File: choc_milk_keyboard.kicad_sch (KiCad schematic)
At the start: 6 parts, among them J1 Conn_01x02_Female, SW1 SW_PUSH, SW2 SW_PUSH, U1 ProMicro

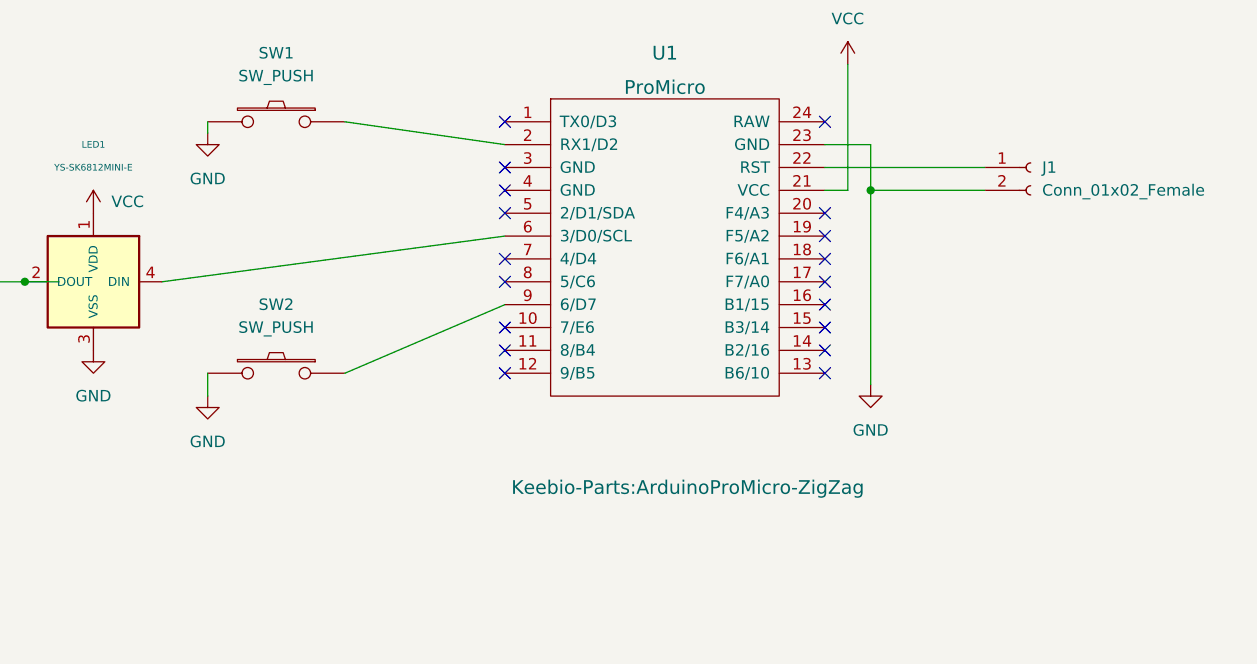
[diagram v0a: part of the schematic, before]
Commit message: Refactored for USB-C ProMicro USB-C is 3mm longer than micro usb Created a new footprint variant
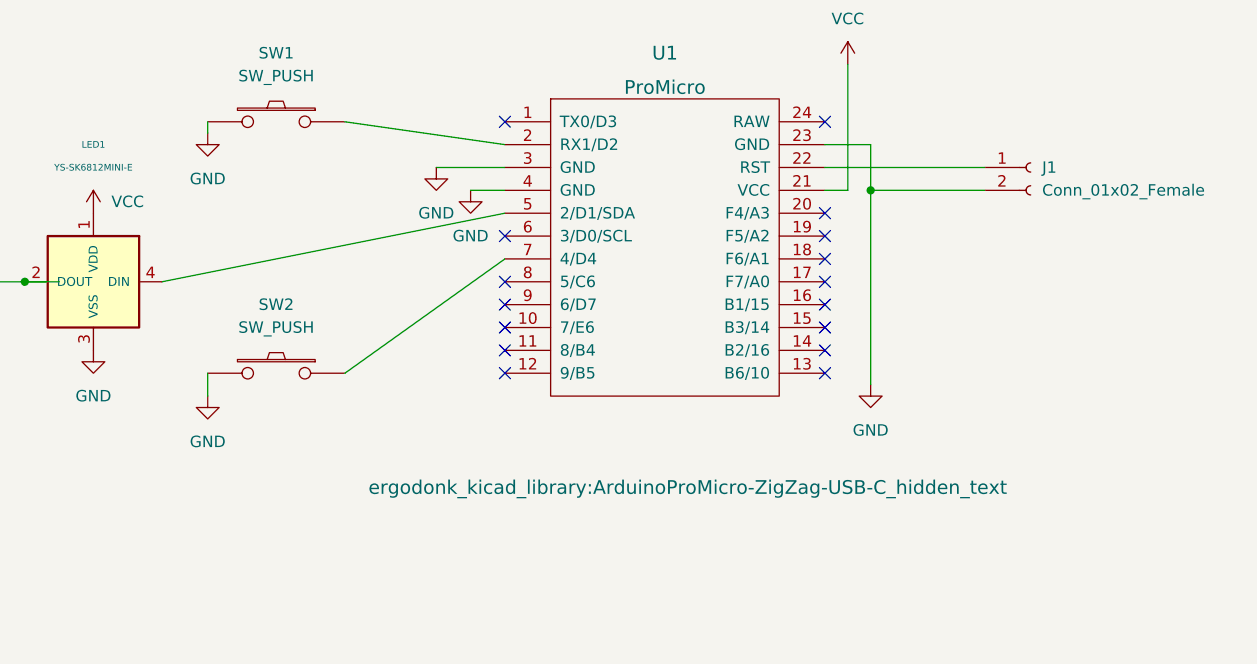
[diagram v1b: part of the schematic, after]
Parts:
- U1: footprint Keebio-Parts:ArduinoProMicro-ZigZag -> ergodonk_kicad_library:ArduinoProMicro-ZigZag-USB-C_hidden_text
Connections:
- net GND: now also U1.3 (GND), U1.4 (GND)
- net at U1.5 (2/D1/SDA): now also LED1.4 (DIN)
- net at U1.6 (3/D0/SCL): no longer LED1.4 (DIN)
- net at U1.7 (4/D4): now also SW2.1
- net at U1.9 (6/D7): no longer SW2.1
- no-connect marks 18 -> 16
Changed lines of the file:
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@@
   (no_connect (at 179.07 99.06))
   (no_connect (at 179.07 101.6))
-  (no_connect (at 143.51 78.74))
-  (no_connect (at 143.51 81.28))
-  (no_connect (at 143.51 83.82))
   (no_connect (at 143.51 96.52))
   (no_connect (at 143.51 99.06))
   (no_connect (at 143.51 101.6))
-  (no_connect (at 143.51 88.9))
   (no_connect (at 143.51 91.44))
-  (wire (pts (xy 125.73 101.6) (xy 143.51 93.98))
-    (stroke (width 0) (type default) (color 0 0 0 0))
-  )
+  (no_connect (at 143.51 93.98))
+  (no_connect (at 143.51 86.36))
   (wire (pts (xy 93.98 91.44) (xy 90.17 91.44))
     (stroke (width 0) (type default) (color 0 0 0 0))
@@
     (stroke (width 0) (type default) (color 0 0 0 0))
   )
+  (wire (pts (xy 135.89 78.74) (xy 143.51 78.74))
+    (stroke (width 0) (type default) (color 0 0 0 0))
+  )
   (wire (pts (xy 184.15 76.2) (xy 184.15 81.28))
     (stroke (width 0) (type default) (color 0 0 0 0))
@@
     (stroke (width 0) (type default) (color 0 0 0 0))
   )
+  (wire (pts (xy 125.73 101.6) (xy 143.51 88.9))
+    (stroke (width 0) (type default) (color 0 0 0 0))
+  )
   (wire (pts (xy 110.49 104.14) (xy 110.49 101.6))
     (stroke (width 0) (type default) (color 0 0 0 0))
@@
     (stroke (width 0) (type default) (color 0 0 0 0))
   )
-  (wire (pts (xy 143.51 86.36) (xy 105.41 91.44))
-    (stroke (width 0) (type default) (color 0 0 0 0))
-  )
   (wire (pts (xy 196.85 81.28) (xy 184.15 81.28))
     (stroke (width 0) (type default) (color 0 0 0 0))
@@
   )
   (wire (pts (xy 179.07 76.2) (xy 184.15 76.2))
+    (stroke (width 0) (type default) (color 0 0 0 0))
+  )
+  (wire (pts (xy 139.7 81.28) (xy 143.51 81.28))
+    (stroke (width 0) (type default) (color 0 0 0 0))
+  )
+  (wire (pts (xy 143.51 83.82) (xy 105.41 91.44))
     (stroke (width 0) (type default) (color 0 0 0 0))
   )
@@
     (pin "1")
   )
+  (symbol (lib_id "power:GND") (at 139.7 81.28 0) (unit 1)
+    (in_bom yes) (on_board yes) (fields_autoplaced)
+    (property "Reference" "#PWR0112" (id 0) (at 139.7 87.63 0)
+      (effects (font (size 1.27 1.27)) hide)
+    )
+    (property "Value" "GND" (id 1) (at 139.7 86.36 0))
+    (property "Footprint" "" (id 2) (at 139.7 81.28 0)
+      (effects (font (size 1.27 1.27)) hide)
+    )
+    (property "Datasheet" "" (id 3) (at 139.7 81.28 0)
+      (effects (font (size 1.27 1.27)) hide)
+    )
+    (pin "1")
+  )
   (symbol (lib_id "kbd:ProMicro") (at 161.29 87.63 0) (unit 1)
     (in_bom yes) (on_board yes) (fields_autoplaced)
@@
       (effects (font (size 1.524 1.524)))
     )
-    (property "Footprint" "Keebio-Parts:ArduinoProMicro-ZigZag" (id 2) (at 163.83 114.3 0)
+    (property "Footprint" "ergodonk_kicad_library:ArduinoProMicro-ZigZag-USB-C_hidden_text" (id 2) (at 163.83 114.3 0)
       (effects (font (size 1.524 1.524)))
     )
@@
     (pin "1")
   )
+  (symbol (lib_id "power:GND") (at 135.89 78.74 0) (unit 1)
+    (in_bom yes) (on_board yes) (fields_autoplaced)
+    (property "Reference" "#PWR0111" (id 0) (at 135.89 85.09 0)
+      (effects (font (size 1.27 1.27)) hide)
+    )
+    (property "Value" "GND" (id 1) (at 135.89 83.82 0))
+    (property "Footprint" "" (id 2) (at 135.89 78.74 0)
+      (effects (font (size 1.27 1.27)) hide)
+    )
+    (property "Datasheet" "" (id 3) (at 135.89 78.74 0)
+      (effects (font (size 1.27 1.27)) hide)
+    )
+    (pin "1")
+  )
   (symbol (lib_id "kbd:YS-SK6812MINI-E") (at 78.74 91.44 0) (mirror y) (unit 1)
     (in_bom yes) (on_board yes)
@@
       (reference "#PWR0110") (unit 1) (value "GND") (footprint "")
     )
+    (path "/5dadfc8f-3ee6-40da-896a-c632534f4a0e"
+      (reference "#PWR0111") (unit 1) (value "GND") (footprint "")
+    )
+    (path "/2e2b6378-1b23-4035-8bf1-41dbdbe8a392"
+      (reference "#PWR0112") (unit 1) (value "GND") (footprint "")
+    )
     (path "/08b252a0-3925-44b6-a676-7cbcf9d3501f"
       (reference "J1") (unit 1) (value "Conn_01x02_Female") (footprint "Connector_PinHeader_2.54mm:PinHeader_1x02_P2.54mm_Vertical")
@@
     )
     (path "/363f4179-68ab-4aea-9f89-f83afdbdb4b7"
-      (reference "U1") (unit 1) (value "ProMicro") (footprint "Keebio-Parts:ArduinoProMicro-ZigZag")
-    )
-  )
+      (reference "U1") (unit 1) (value "ProMicro") (footprint "ergodonk_kicad_library:ArduinoProMicro-ZigZag-USB-C_hidden_text")
+    )
+  )

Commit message: Added 3d models, flipped pro micro
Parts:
- SW1, SW2: footprint ergodonk_kicad_library:Low-Profile-Choc-MX -> ergodonk_kicad_library:Low-Profile-Choc-MX_no_text
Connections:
- net at U1.20 (F4/A3): now also LED1.4 (DIN)
- net at U1.5 (2/D1/SDA): no longer LED1.4 (DIN)
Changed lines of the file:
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@@
+    (stroke (width 0) (type default) (color 0 0 0 0))
+  )
+  (wire (pts (xy 105.41 91.44) (xy 179.07 83.82))
     (stroke (width 0) (type default) (color 0 0 0 0))
   )
@@
   )
   (wire (pts (xy 139.7 81.28) (xy 143.51 81.28))
-    (stroke (width 0) (type default) (color 0 0 0 0))
-  )
-  (wire (pts (xy 143.51 83.82) (xy 105.41 91.44))
     (stroke (width 0) (type default) (color 0 0 0 0))
   )
@@
     (property "Reference" "SW2" (id 0) (at 118.11 93.98 0))
     (property "Value" "SW_PUSH" (id 1) (at 118.11 96.52 0))
-    (property "Footprint" "ergodonk_kicad_library:Low-Profile-Choc-MX" (id 2) (at 118.11 101.6 0)
+    (property "Footprint" "ergodonk_kicad_library:Low-Profile-Choc-MX_no_text" (id 2) (at 118.11 101.6 0)
       (effects (font (size 1.27 1.27)) hide)
     )
@@
     (property "Reference" "SW1" (id 0) (at 118.11 66.04 0))
     (property "Value" "SW_PUSH" (id 1) (at 118.11 68.58 0))
-    (property "Footprint" "ergodonk_kicad_library:Low-Profile-Choc-MX" (id 2) (at 118.11 73.66 0)
+    (property "Footprint" "ergodonk_kicad_library:Low-Profile-Choc-MX_no_text" (id 2) (at 118.11 73.66 0)
       (effects (font (size 1.27 1.27)) hide)
     )
@@
     )
     (path "/969504db-c0a2-490d-9b85-23f769a5df17"
-      (reference "SW1") (unit 1) (value "SW_PUSH") (footprint "ergodonk_kicad_library:Low-Profile-Choc-MX")
+      (reference "SW1") (unit 1) (value "SW_PUSH") (footprint "ergodonk_kicad_library:Low-Profile-Choc-MX_no_text")
     )
     (path "/3f208ee3-248a-49f4-af2f-edd1fe595888"
-      (reference "SW2") (unit 1) (value "SW_PUSH") (footprint "ergodonk_kicad_library:Low-Profile-Choc-MX")
+      (reference "SW2") (unit 1) (value "SW_PUSH") (footprint "ergodonk_kicad_library:Low-Profile-Choc-MX_no_text")
     )
     (path "/363f4179-68ab-4aea-9f89-f83afdbdb4b7"

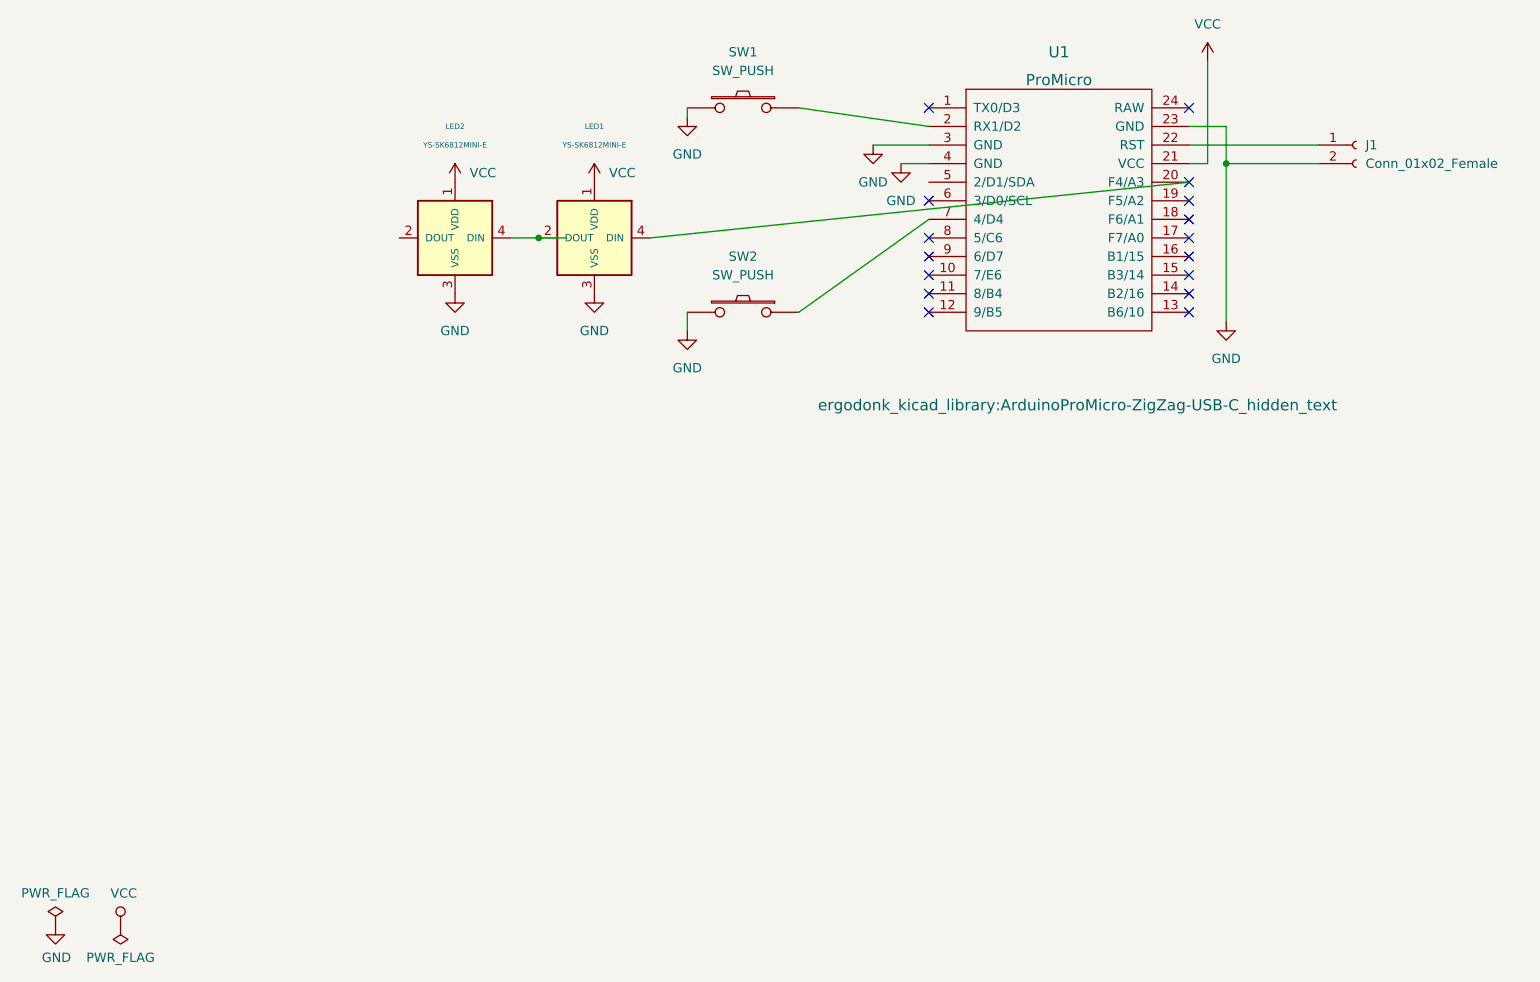
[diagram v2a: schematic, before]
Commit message: Revised Choc footprint and added logo There are 2 Choc V2 variants - one has an extra non-functional pin. Added drawings and added hole to footprint. Flipped switches and Leds to make routing around hole cleaner Added multilayer logo
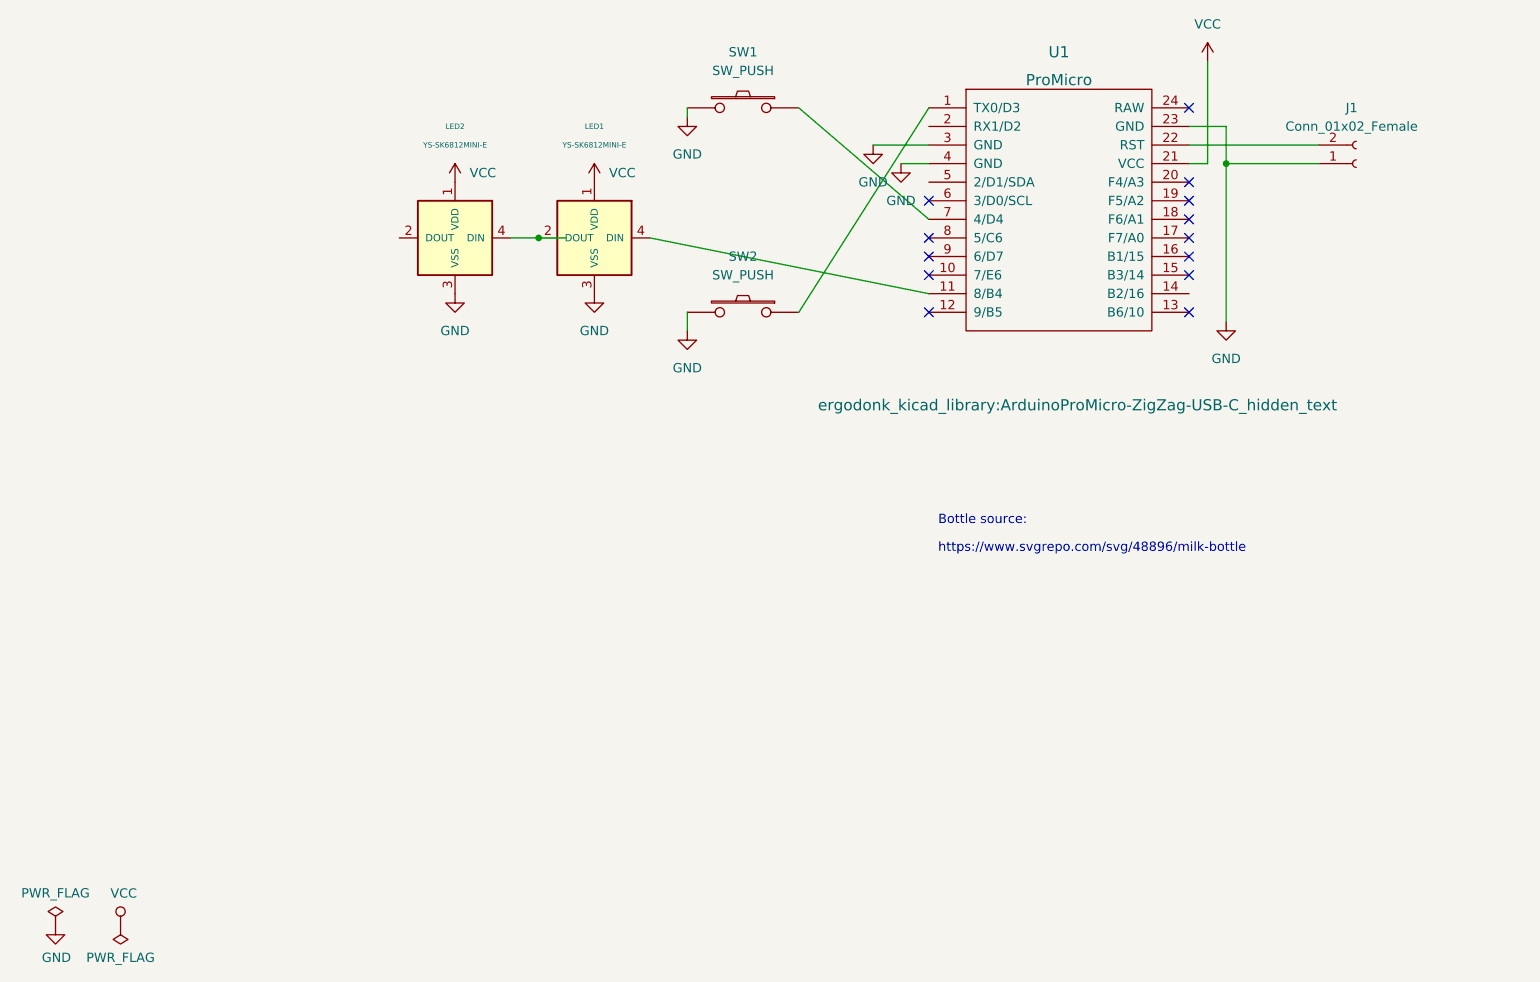
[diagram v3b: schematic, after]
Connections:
- net GND: now also J1.1 (Pin_1); no longer J1.2 (Pin_2)
- net at U1.22 (RST): now also J1.2 (Pin_2); no longer J1.1 (Pin_1)
- net at U1.1 (TX0/D3): now also SW2.1
- net at U1.11 (8/B4): now also LED1.4 (DIN)
- net at U1.2 (RX1/D2): no longer SW1.1
- net at U1.20 (F4/A3): no longer LED1.4 (DIN)
- net at U1.7 (4/D4): now also SW1.1; no longer SW2.1
- no-connect marks 16 -> 13
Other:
- note added: "Bottle source:"
- note added: "https://www.svgrepo.com/svg/48896/milk-bottle"
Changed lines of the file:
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@@
   (junction (at 90.17 91.44) (diameter 0) (color 0 0 0 0)
   )
-  (no_connect (at 143.51 73.66))
   (no_connect (at 179.07 83.82))
   (no_connect (at 179.07 86.36))
@@
   (no_connect (at 179.07 93.98))
   (no_connect (at 179.07 96.52))
-  (no_connect (at 179.07 99.06))
   (no_connect (at 179.07 101.6))
   (no_connect (at 143.51 96.52))
-  (no_connect (at 143.51 99.06))
   (no_connect (at 143.51 101.6))
   (no_connect (at 143.51 91.44))
@@
   (no_connect (at 143.51 86.36))
   (wire (pts (xy 93.98 91.44) (xy 90.17 91.44))
-    (stroke (width 0) (type default) (color 0 0 0 0))
-  )
-  (wire (pts (xy 125.73 73.66) (xy 143.51 76.2))
     (stroke (width 0) (type default) (color 0 0 0 0))
   )
@@
     (stroke (width 0) (type default) (color 0 0 0 0))
   )
-  (wire (pts (xy 179.07 78.74) (xy 196.85 78.74))
+  (wire (pts (xy 110.49 104.14) (xy 110.49 101.6))
     (stroke (width 0) (type default) (color 0 0 0 0))
   )
-  (wire (pts (xy 125.73 101.6) (xy 143.51 88.9))
-    (stroke (width 0) (type default) (color 0 0 0 0))
-  )
-  (wire (pts (xy 105.41 91.44) (xy 179.07 83.82))
-    (stroke (width 0) (type default) (color 0 0 0 0))
-  )
-  (wire (pts (xy 110.49 104.14) (xy 110.49 101.6))
+  (wire (pts (xy 179.07 78.74) (xy 196.85 78.74))
     (stroke (width 0) (type default) (color 0 0 0 0))
   )
@@
   )
   (wire (pts (xy 110.49 74.93) (xy 110.49 73.66))
+    (stroke (width 0) (type default) (color 0 0 0 0))
+  )
+  (wire (pts (xy 105.41 91.44) (xy 143.51 99.06))
     (stroke (width 0) (type default) (color 0 0 0 0))
   )
@@
     (stroke (width 0) (type default) (color 0 0 0 0))
   )
-  (symbol (lib_id "Connector:Conn_01x02_Female") (at 201.93 78.74 0) (unit 1)
+  (wire (pts (xy 125.73 101.6) (xy 143.51 73.66))
+    (stroke (width 0) (type default) (color 0 0 0 0))
+  )
+  (wire (pts (xy 125.73 73.66) (xy 143.51 88.9))
+    (stroke (width 0) (type default) (color 0 0 0 0))
+  )
+  (text "https://www.svgrepo.com/svg/48896/milk-bottle" (at 144.78 134.62 0)
+    (effects (font (size 1.27 1.27)) (justify left bottom))
+  )
+  (text "Bottle source:" (at 144.78 130.81 0)
+    (effects (font (size 1.27 1.27)) (justify left bottom))
+  )
+  (symbol (lib_id "Connector:Conn_01x02_Female") (at 201.93 81.28 0) (mirror x) (unit 1)
     (in_bom yes) (on_board yes) (fields_autoplaced)
-    (property "Reference" "J1" (id 0) (at 203.2 78.7399 0)
-      (effects (font (size 1.27 1.27)) (justify left))
-    )
-    (property "Value" "Conn_01x02_Female" (id 1) (at 203.2 81.2799 0)
-      (effects (font (size 1.27 1.27)) (justify left))
-    )
-    (property "Footprint" "Connector_PinHeader_2.54mm:PinHeader_1x02_P2.54mm_Vertical" (id 2) (at 201.93 78.74 0)
+    (property "Reference" "J1" (id 0) (at 201.295 73.66 0))
+    (property "Value" "Conn_01x02_Female" (id 1) (at 201.295 76.2 0))
+    (property "Footprint" "Connector_PinHeader_2.54mm:PinHeader_1x02_P2.54mm_Vertical" (id 2) (at 201.93 81.28 0)
       (effects (font (size 1.27 1.27)) hide)
     )
-    (property "Datasheet" "~" (id 3) (at 201.93 78.74 0)
+    (property "Datasheet" "~" (id 3) (at 201.93 81.28 0)
       (effects (font (size 1.27 1.27)) hide)
     )

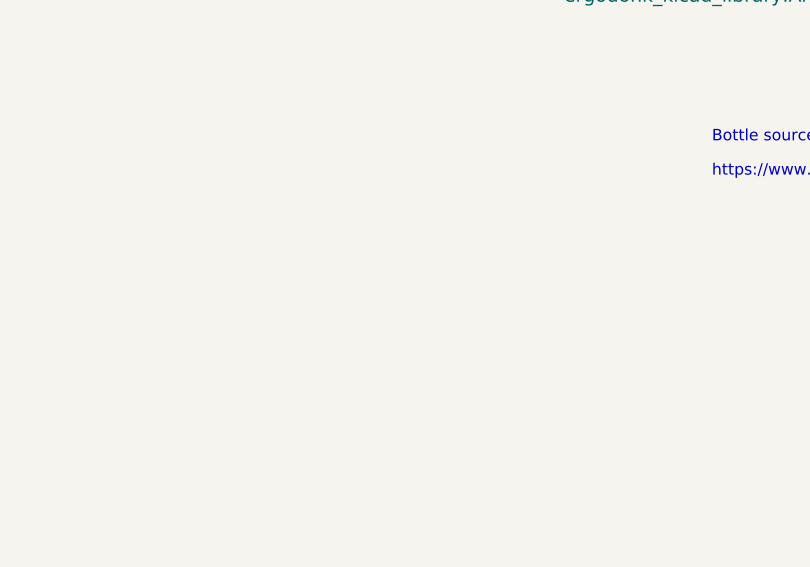
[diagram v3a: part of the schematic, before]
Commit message: Logo tweak for production and added todo list
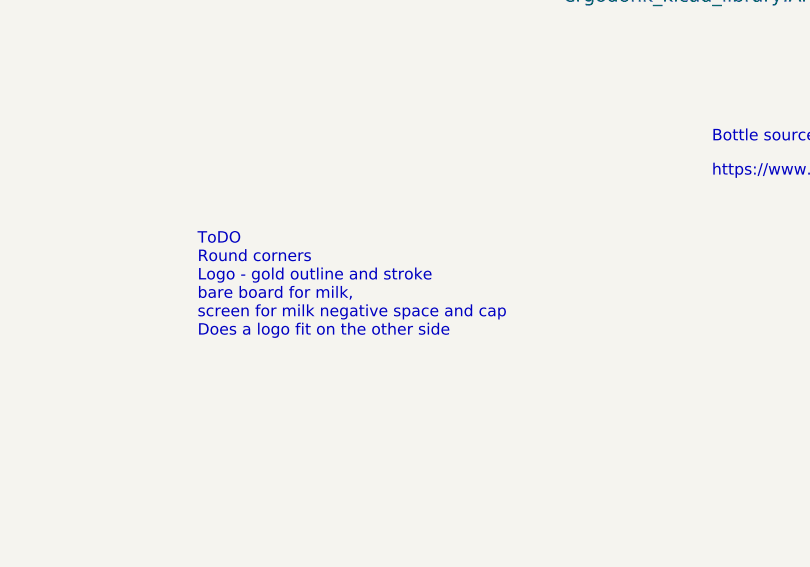
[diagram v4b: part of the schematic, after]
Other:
- note added: "ToDO Round corners Logo - gold outline and stroke bare board for milk, screen for milk negative space and cap Does a logo fit on the other side"
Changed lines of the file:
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@@
     (stroke (width 0) (type default) (color 0 0 0 0))
+  )
+  (text "ToDO\nRound corners\nLogo - gold outline and stroke\nbare board for milk,\nscreen for milk negative space and cap\nDoes a logo fit on the other side"
+    (at 87.63 152.4 0)
+    (effects (font (size 1.27 1.27)) (justify left bottom))
   )
   (text "https://www.svgrepo.com/svg/48896/milk-bottle" (at 144.78 134.62 0)
